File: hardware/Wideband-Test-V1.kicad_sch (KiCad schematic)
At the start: 284 parts, among them IC1 LMX2592RHAT, IC2 BU7205HFV-TR, IC3 GRF3042, IC4 OPA2673IRGVR, IC5 BU7205HFV-TR, IC6 BU7205HFV-TR, IC7 LIF-MD6000-6UMG64I, J1 RJ45, J2 Conn_01x02_Pin, J3 Conn_01x04_Pin, J4 Conn_01x04_Pin, J5 Conn_01x04_Pin, J6 Conn_01x04_Pin, J7 Conn_01x02_Pin, J8 USB_B_Micro, Q1 MMBFJ113, Q10 MMBFJ113, Q11 MMBFJ113, Q12 BFP840ESD, Q13 BFP840ESD, Q14 BFP840ESD, Q15 BFP840ESD, Q16 BFP840ESD, Q2 MMBFJ113, Q3 MMBFJ113, Q4 MMBFJ113, Q5 MMBFJ113, Q6 MMBFJ113, Q7 BFP840ESD, Q8 MMBFJ113, Q9 MMBFJ113, T1 CX2041NLT, U1 AD9215BCPZ-105, U2 BGA614H6327XTSA1, U3 LD1117V-3V3, U4 BGA614H6327XTSA1, U5 AP7381-50SA-7, U6 KSZ9031RNXCA, U7 RP2040, U8 8M-Q, Y1 Crystal_GND24, Y2 12M, Y3 25M

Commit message: 1.2
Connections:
- now unconnected: Q10.3 (G), Q11.3 (G), Q8.3 (G), Q9.3 (G), U7.17 (GPIO14), U7.18 (GPIO15)
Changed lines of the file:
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@@
 	)
 	(junction
-		(at 552.45 297.18)
-		(diameter 0)
-		(color 0 0 0 0)
-	)
-	(junction
 		(at 441.96 448.31)
 		(diameter 0)
@@
 	)
 	(junction
-		(at 588.01 414.02)
-		(diameter 0)
-		(color 0 0 0 0)
-	)
-	(junction
 		(at 264.16 264.16)
 		(diameter 0)
@@
 	(wire
 		(pts
-			(xy 577.85 297.18) (xy 552.45 297.18)
-		)
-		(stroke
-			(width 0)
-			(type default)
-		)
-	)
-	(wire
-		(pts
 			(xy 427.99 191.77) (xy 426.72 191.77)
 		)
@@
 	(wire
 		(pts
-			(xy 557.53 322.58) (xy 552.45 322.58)
-		)
-		(stroke
-			(width 0)
-			(type default)
-		)
-	)
-	(wire
-		(pts
 			(xy 290.83 339.09) (xy 290.83 344.17)
 		)
@@
 	(wire
 		(pts
-			(xy 552.45 322.58) (xy 552.45 297.18)
-		)
-		(stroke
-			(width 0)
-			(type default)
-		)
-	)
-	(wire
-		(pts
 			(xy 210.82 430.53) (xy 213.36 430.53)
 		)
@@
 	(wire
 		(pts
+			(xy 552.45 284.48) (xy 552.45 304.8)
+		)
+		(stroke
+			(width 0)
+			(type default)
+		)
+	)
+	(wire
+		(pts
 			(xy 285.75 354.33) (xy 294.64 354.33)
 		)
@@
 	(wire
 		(pts
-			(xy 575.31 433.07) (xy 588.01 433.07)
-		)
-		(stroke
-			(width 0)
-			(type default)
-		)
-	)
-	(wire
-		(pts
 			(xy 283.21 369.57) (xy 283.21 377.19)
 		)
@@
 	(wire
 		(pts
-			(xy 588.01 433.07) (xy 588.01 414.02)
-		)
-		(stroke
-			(width 0)
-			(type default)
-		)
-	)
-	(wire
-		(pts
 			(xy 486.41 378.46) (xy 486.41 379.73)
 		)
@@
 	(wire
 		(pts
-			(xy 556.26 414.02) (xy 588.01 414.02)
-		)
-		(stroke
-			(width 0)
-			(type default)
-		)
-	)
-	(wire
-		(pts
 			(xy 544.83 345.44) (xy 544.83 351.79)
 		)
@@
 	(wire
 		(pts
-			(xy 552.45 297.18) (xy 552.45 284.48)
-		)
-		(stroke
-			(width 0)
-			(type default)
-		)
-	)
-	(wire
-		(pts
 			(xy 462.28 416.56) (xy 452.12 416.56)
 		)
@@
 		)
 		(stroke
-			(width 0)
-			(type default)
-		)
-	)
-	(wire
-		(pts
-			(xy 577.85 311.15) (xy 577.85 297.18)
-		)
-		(stroke

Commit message: hardwares
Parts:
- removed J7: Conn_01x02_Pin, Connector_PinHeader_2.54mm:PinHeader_1x02_P2.54mm_Vertical, symbol Connector:Conn_01x02_Pin
- removed Q10, Q11, Q8, Q9: MMBFJ113, Package_DFN_QFN:Diodes_DFN1006-3, symbol Transistor_FET:MMBFJ113
- added U10, U11, U12, U13, U14, U9: BGS12WN6E6327, Package_LGA:Infineon_PG-TSNP-6-10_0.7x1.1mm_0.7x1.1mm_P0.4mm, symbol RF_Switch:BGS12WN6E6327
- AE1, AE2, AE3: footprint (none) -> Connector_Coaxial:SMA_Molex_73251-2200_Horizontal
- T1: footprint KiCad:CX2041NLT -> Filter:Filter_SAW-6_3.8x3.8mm
- TR1, TR2, TR3: footprint Package_DIP:SMDIP-6_W7.62mm -> MABA-011108:MABA011108
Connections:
- net +3V3: now also U10.4 (VDD), U11.4 (VDD), U12.4 (VDD), U13.4 (VDD), U14.4 (VDD), U9.4 (VDD)
- net ANT123+: now also U10.3 (RF1), U12.1 (RF2)
- net ANT123-: now also U11.1 (RF2), U9.3 (RF1)
- net ANT2+: now also U9.5 (RFIN)
- net ANT2-: now also U10.5 (RFIN)
- net ANT3+: now also U7.31 (GPIO20), U11.5 (RFIN)
- net ANT3-: now also U7.32 (GPIO21), U12.5 (RFIN)
- net GND: now also AE3.2 (PCB_Trace), C6.2, IC1.4 (GND_2), IC1.6 (GND_3), U10.1 (RF2), U10.2 (GND), U11.2 (GND), U11.3 (RF1), U12.2 (GND), U12.3 (RF1), U13.2 (GND), U13.3 (RF1), U14.2 (GND), U14.3 (RF1), U9.1 (RF2), U9.2 (GND)
- net INAMP+: now also U13.1 (RF2); no longer U2.3 (OUT)
- net INAMP-: now also U14.1 (RF2); no longer U4.3 (OUT)
- net at U7.37 (GPIO25): now also U13.6 (CTRL), U14.6 (CTRL)
- net at U7.17 (GPIO14): now also U11.6 (CTRL), U12.6 (CTRL)
- net at U7.18 (GPIO15): now also U10.6 (CTRL), U9.6 (CTRL)
- new net: U14.5 (RFIN), U4.3 (OUT)
- new net: U13.5 (RFIN), U2.3 (OUT)
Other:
- moved on the sheet: C102, C79, C81, C82, C83, C84, IC3, IC4, IC5, IC6, L1, Q5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

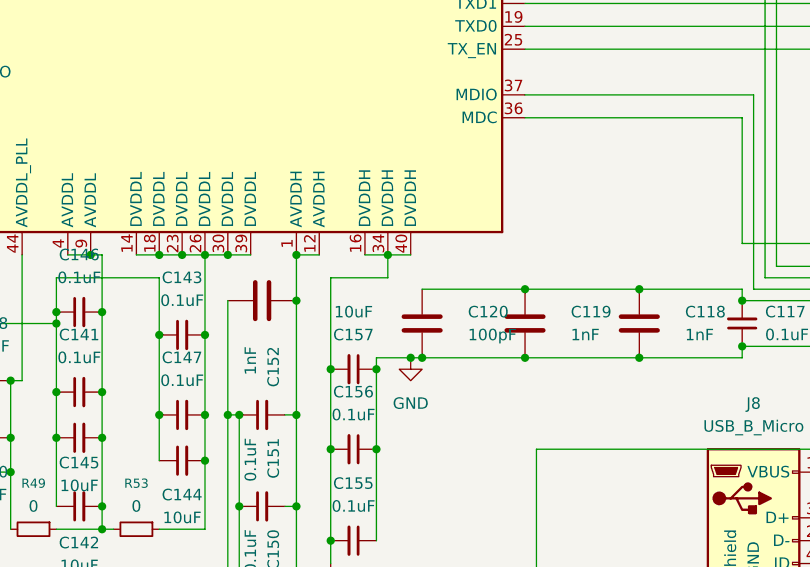
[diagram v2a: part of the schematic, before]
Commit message: Address issue 12 FFT receive path blockers
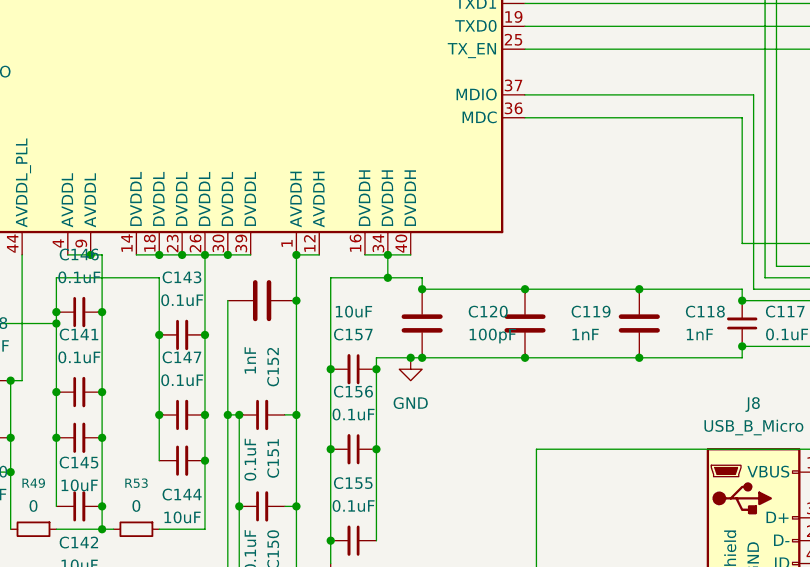
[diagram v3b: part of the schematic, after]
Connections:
- net at C113.2, C114.2, C115.2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: now also C155.2, C156.2, C157.2, R55.1, U6.16 (DVDDH), U6.34 (DVDDH), U6.40 (DVDDH)
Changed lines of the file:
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@@
 	)
 	(junction
+		(at 237.49 434.34)
+		(diameter 0)
+		(color 0 0 0 0)
+	)
+	(junction
 		(at 515.62 421.64)
 		(diameter 0)
@@
 	)
 	(junction
+		(at 233.68 433.07)
+		(diameter 0)
+		(color 0 0 0 0)
+	)
+	(junction
 		(at 452.12 453.39)
 		(diameter 0)
@@
 	(wire
 		(pts
+			(xy 233.68 433.07) (xy 237.49 433.07)
+		)
+		(stroke
+			(width 0)
+			(type default)
+		)
+	)
+	(wire
+		(pts
 			(xy 515.62 405.13) (xy 515.62 421.64)
 		)
@@
 		)
 		(stroke
+			(width 0)
+			(type default)
+		)
+	)
+	(wire
+		(pts
+			(xy 237.49 433.07) (xy 237.49 434.34)
+		)
+		(stroke
